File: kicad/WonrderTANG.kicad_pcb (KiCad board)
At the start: 2 copper layers, 101.6 x 90.2 mm, 31 parts, among them CON1 MSX-CONNECTOR, J1 Conn_02x01, J2 AudioJack3, J3 Conn_02x01, Q1 2N3904, U1 SN74LVC245AN, U2 SN74LVC245AN, U3 SN74LVC245AN, U4 SN74LVC245AN, U5 Tang_Nano_20k, U6 SN74LVC245AN

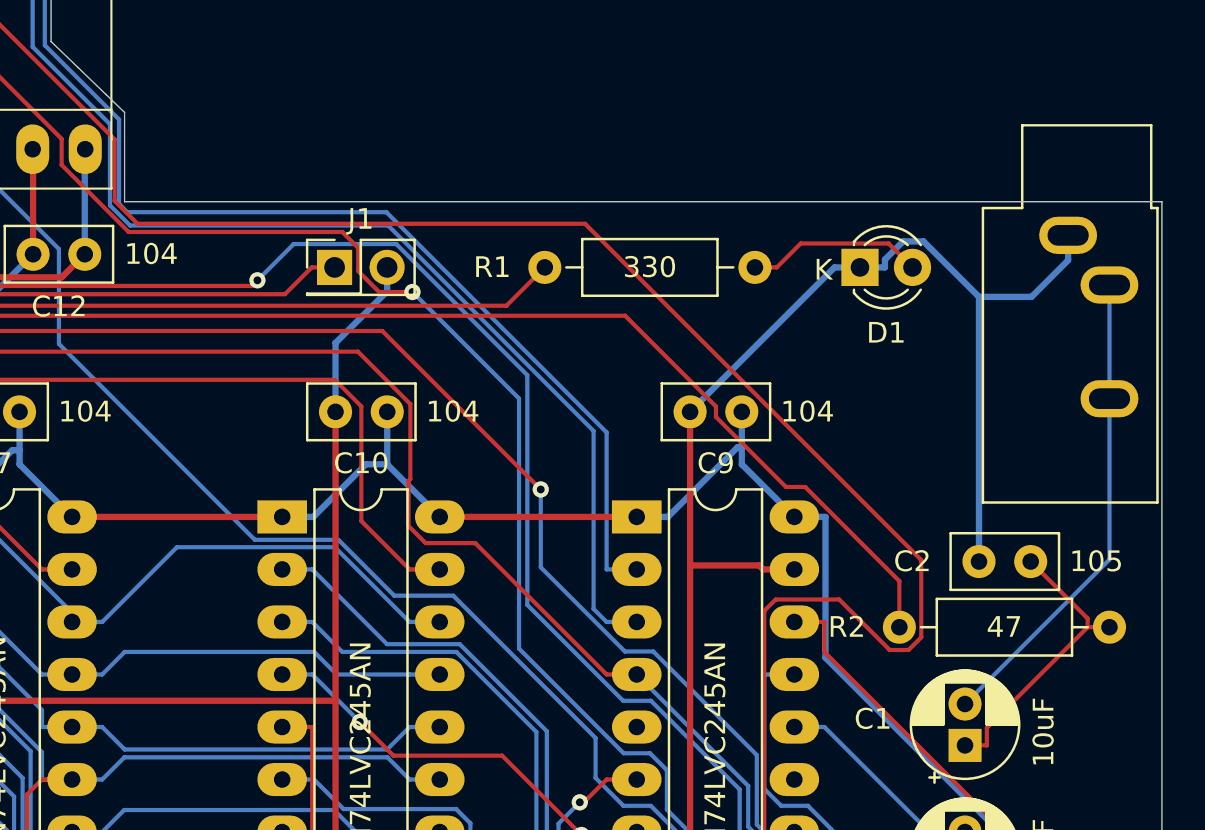
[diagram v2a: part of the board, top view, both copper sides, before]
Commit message: [kicad] Use alternate audio connector SJ1-3525N
Exchange the SJ1-3533NG mono audio connector with the more common
(at least in Europe and some large asian shops) SJ1-3525N stereo
connector, keeping the same orientation.
To fit the new connector the board led is slightly moved too.
This modification also allows to keep the audio connector within
the standard cartridge case depth.

Signed-off-by: Albert Herranz <albert_herranz@yahoo.es>
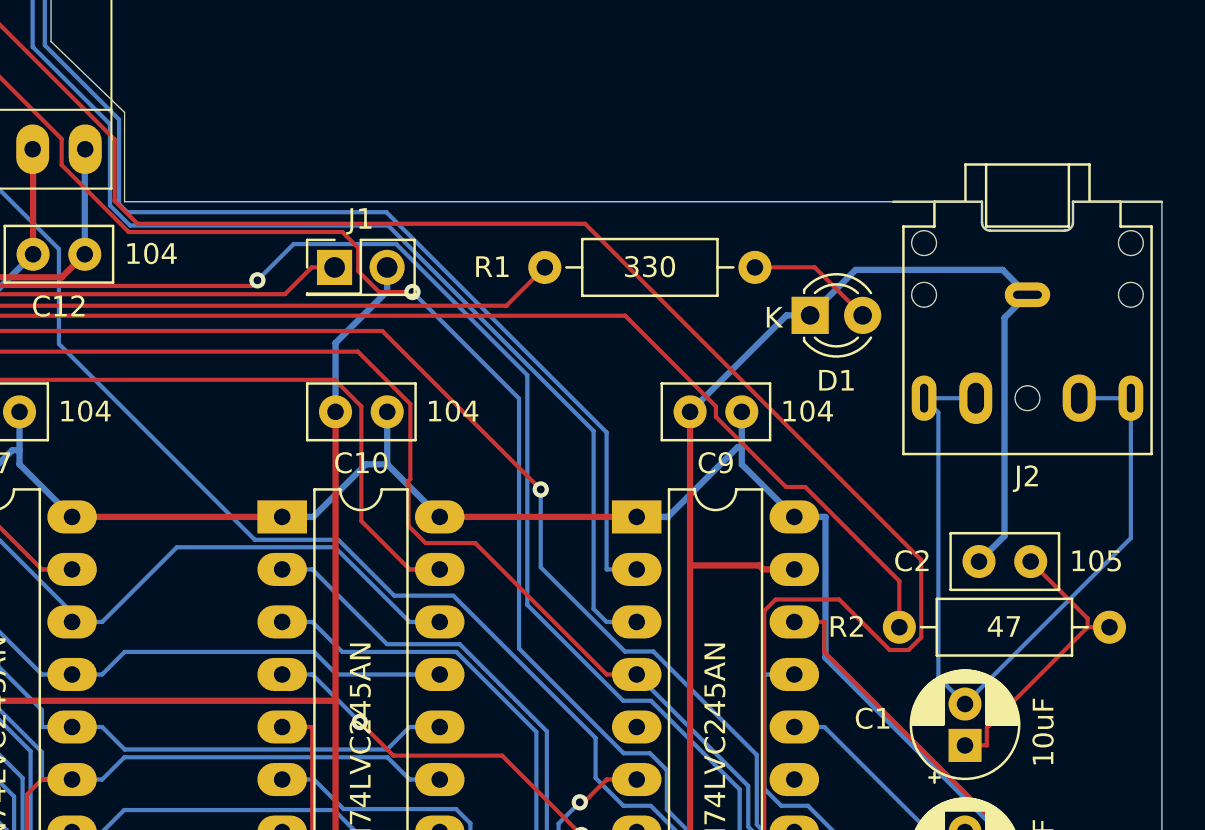
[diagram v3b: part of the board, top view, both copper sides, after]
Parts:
- J2: footprint Connector_Audio:Jack_3.5mm_CUI_SJ1-3533NG_Horizontal -> Connector_Audio:Jack_3.5mm_CUI_SJ1-3525N_Horizontal
- moved J2 3.48 mm to (151.6, 82.6), turned to 180 degrees
- moved D1 3.35 mm to (141.1, 83.6)
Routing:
- net Net-(C1-Pad2): track 23.2 -> 38.7 mm
- net GND: track 406.2 -> 402.0 mm
- net Net-(D1-A): track 8.58 -> 6.17 mm
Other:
- outline, holes or cut-outs redrawn

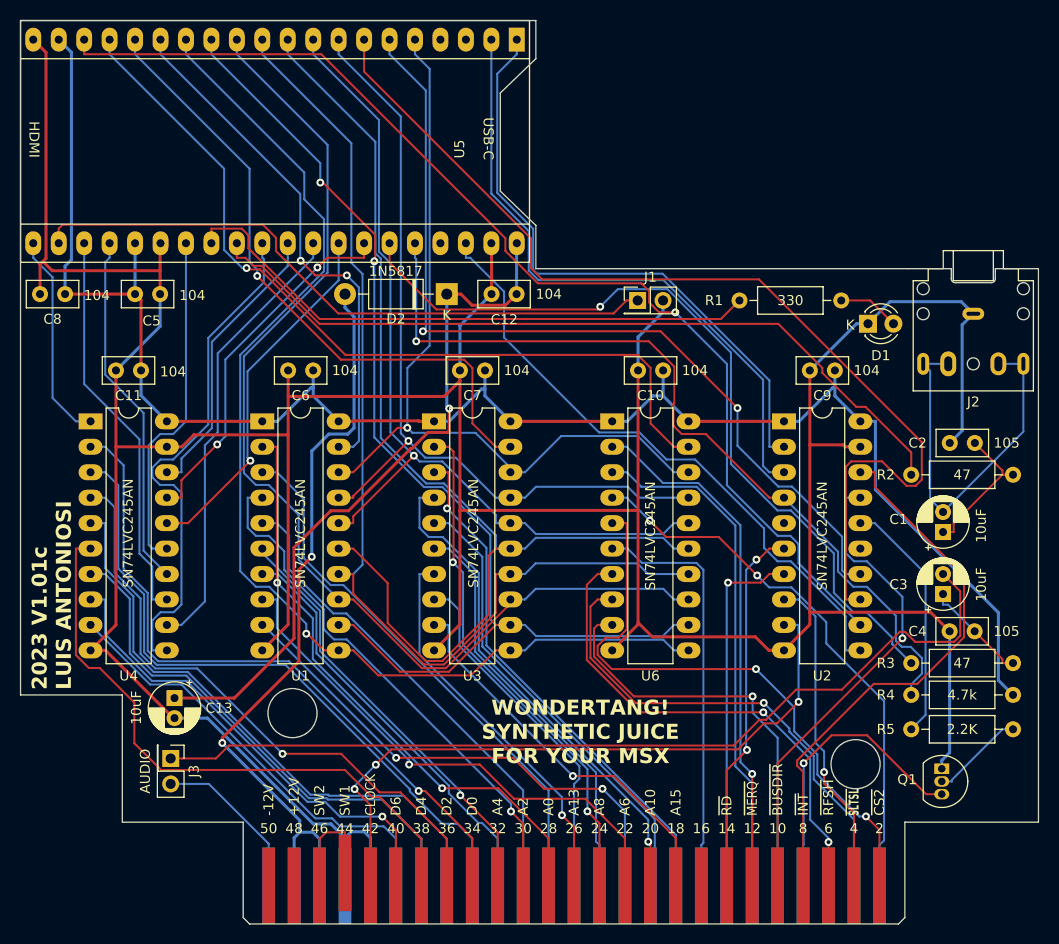
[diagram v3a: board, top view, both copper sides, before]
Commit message: [kicad] Add copper fill for GND
Add copper fill on the bottom layer for GND.
It may provide added signal integrity.

Signed-off-by: Albert Herranz <albert_herranz@yahoo.es>
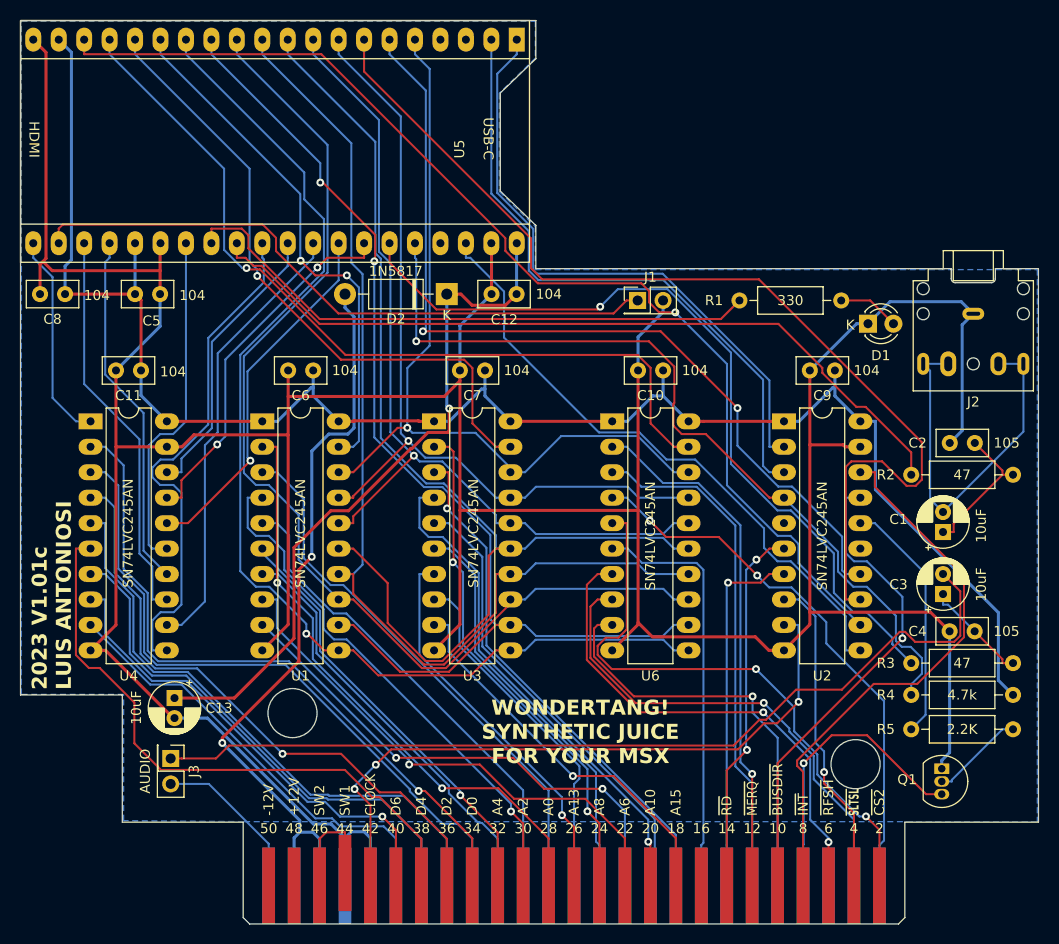
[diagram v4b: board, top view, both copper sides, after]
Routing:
- added copper zone on B.Cu, net GND
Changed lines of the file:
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@@
+    )
+  )
+  (zone (net 2) (net_name "GND") (layer "B.Cu") (hatch edge 0.5)
+    (connect_pads (clearance 0.3508))
+    (min_thickness 0.25) (filled_areas_thickness no)
+    (fill yes (thermal_gap 0.5) (thermal_bridge_width 0.5))
+    (polygon
+      (pts
+        (xy 56.6 53.4)
+        (xy 107.9 53.4)
+        (xy 107.9 57.1)
+        (xy 104.3 60.6)
+        (xy 104.3 70.4)
+        (xy 107.9 73.9)
+        (xy 107.9 78.2)
+        (xy 158 78.2)
+        (xy 158 133.3)
+        (xy 78.8 133.3)
+        (xy 66.8 133.2)
+        (xy 66.8 120.6)
+        (xy 56.6 120.6)
+      )
     )
   )

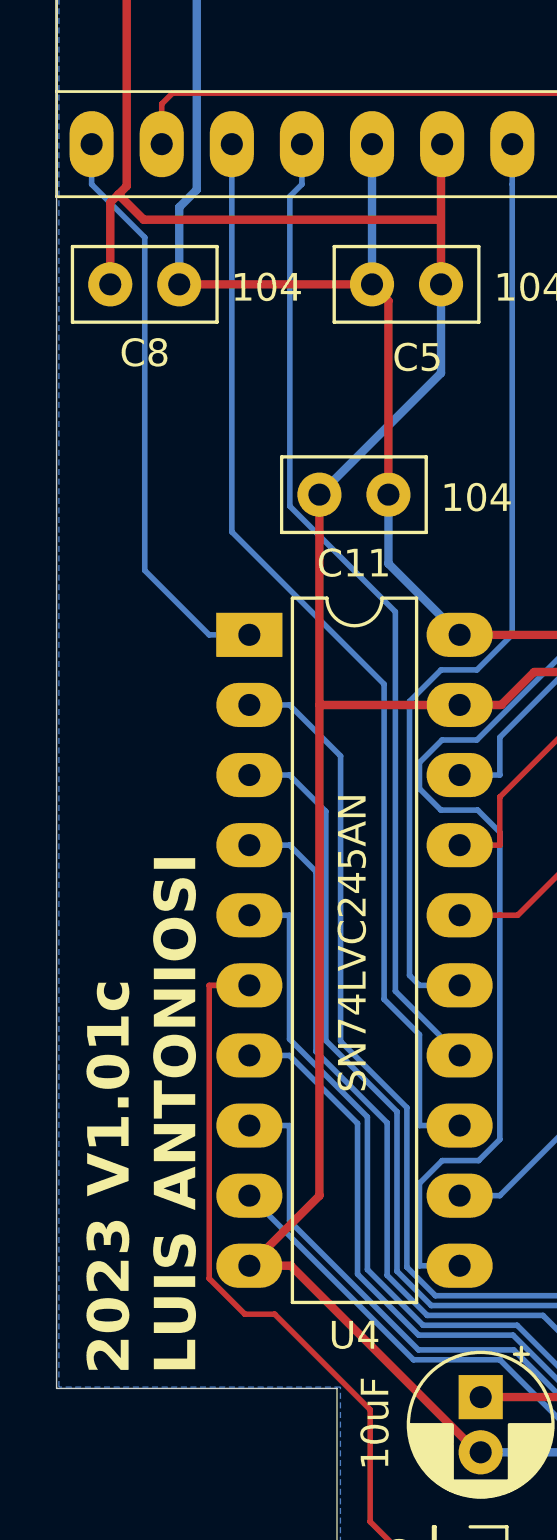
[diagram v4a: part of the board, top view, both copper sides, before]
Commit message: [kicad] Mark board as V1.01c.F1 fork
Identify this board as a new fork to avoid confusion with the stock
board by slightly changing the silkscreen identification.

Signed-off-by: Albert Herranz <albert_herranz@yahoo.es>
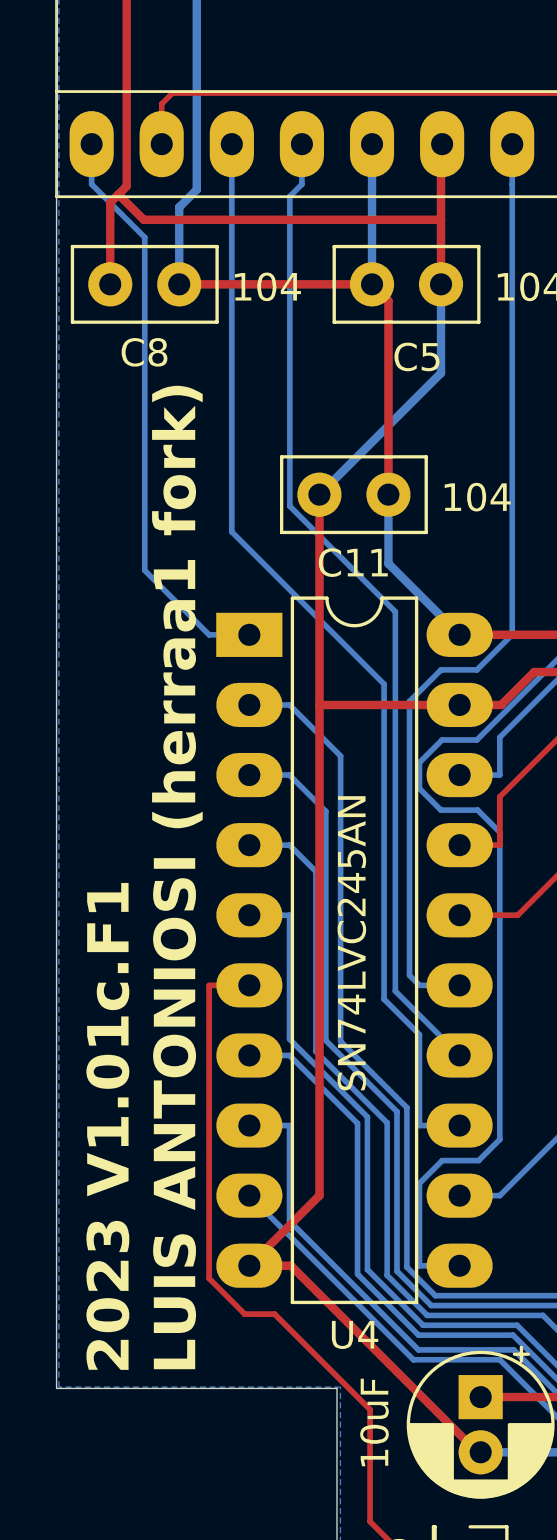
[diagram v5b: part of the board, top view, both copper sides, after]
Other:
- board text added: "2023 V1.01c.F1 LUIS ANTONIOSI (herraa1 fork)"
- board text removed: "2023 V1.01c LUIS ANTONIOSI"
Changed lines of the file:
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@@
     (effects (font (size 1 1) (thickness 0.15)))
   )
-  (gr_text "2023 V1.01c\nLUIS ANTONIOSI" (at 61.722 120.142 90) (layer "F.SilkS")
+  (gr_text "2023 V1.01c.F1\nLUIS ANTONIOSI (herraa1 fork)" (at 61.722 120.142 90) (layer "F.SilkS")
     (effects (font (size 1.5 1.5) (thickness 0.3) bold) (justify left bottom))
   )
